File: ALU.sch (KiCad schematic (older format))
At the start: 54 parts, among them U501 74LS86AN, U502 74HCT32N, U503 74HCT32N, U504 74LS04, U505 74HCT157N, U506 74LS86AN, U507 74LS153, U508 74LS283N, U509 74HCT08N, U510 74HCT574N, U511 74LS283N, U512 74HCT541N, U513 74HCT08N, U514 74HCT574N, U515 74HCT541N, U516 74HCT08N, U517 74HCT74N, U518 74HCT74N

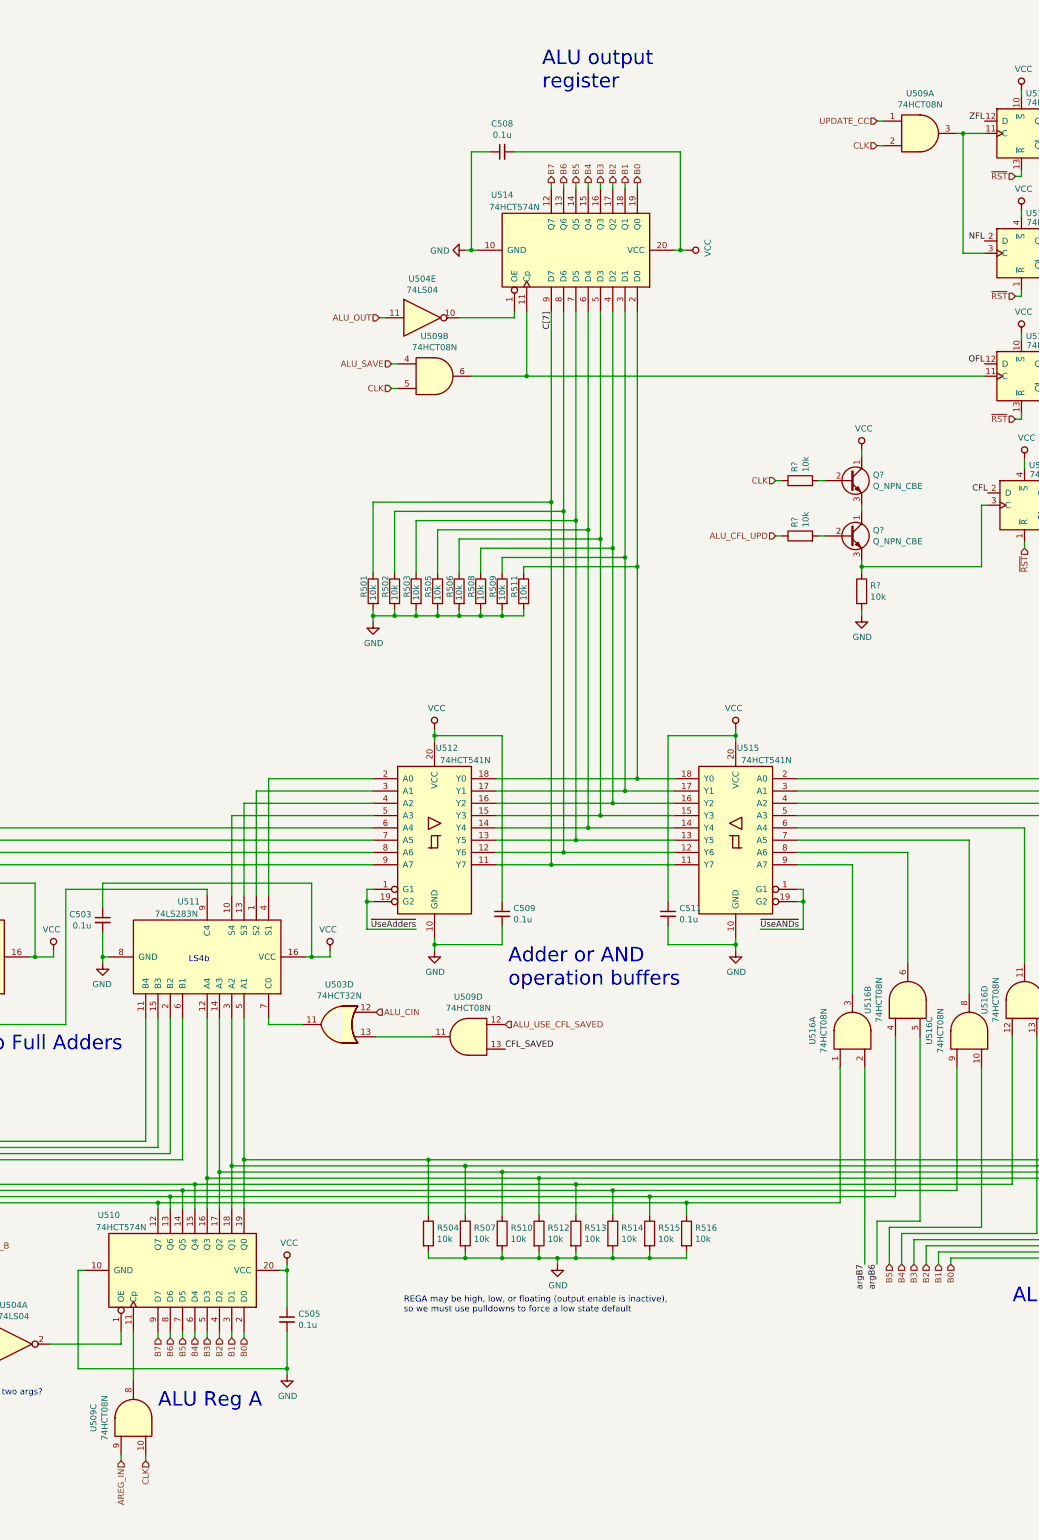
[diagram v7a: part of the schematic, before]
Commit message: Rearranged some generic logic gates in ALU to match physical net connections on the breadboard.
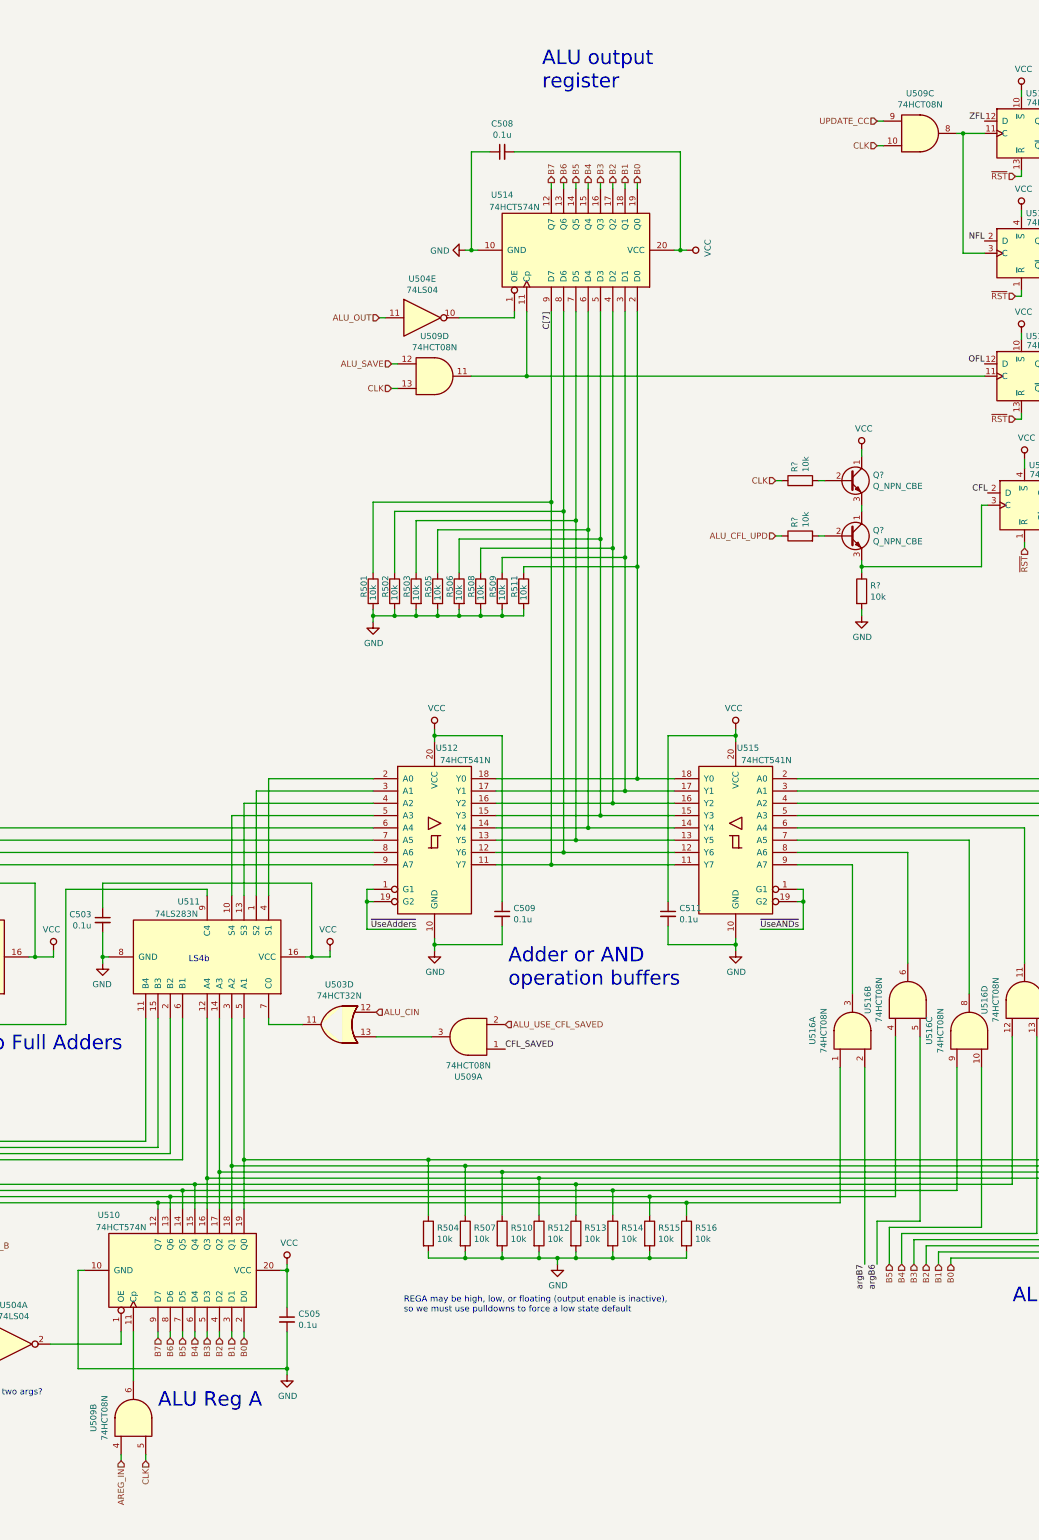
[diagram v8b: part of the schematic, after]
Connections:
- net ALU_SAVE: now also U509.12; no longer U509.4
- net ALU_USE_CFL_SAVED: now also U509.2; no longer U509.12
- net AREG_IN: now also U509.4; no longer U509.9
- net CFL_SAVED: now also U509.1; no longer U509.13
- net CLK: now also U509.13; no longer U509.2
- net UPDATE_CC: now also U509.9; no longer U509.1
- net at U514.11 (Cp), U517.11 (C): now also U509.11; no longer U509.6
- net at U518.11 (C), U518.3 (C): now also U509.8; no longer U509.3
- net at U503.13: now also U509.3; no longer U509.11
- net at U510.11 (Cp): now also U509.6; no longer U509.8
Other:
- moved on the sheet: U509A, U509B, U509C, U509D
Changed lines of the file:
@@
 L Breadboard_CPU-rescue:74LS08-74xx U509
 U 4 1 610C6B10
-P 10325 9600
-F 0 "U509" H 10325 9925 50  0000 C CNN
-F 1 "74HCT08N" H 10325 9834 50  0000 C CNN
-F 2 "" H 10325 9600 50  0001 C CNN
-F 3 "http://www.ti.com/lit/gpn/sn74LS08" H 10325 9600 50  0001 C CNN
-	4    10325 9600
-	-1   0    0    -1
+P 10050 4225
+F 0 "U509" H 10050 4550 50  0000 C CNN
+F 1 "74HCT08N" H 10050 4459 50  0000 C CNN
+F 2 "" H 10050 4225 50  0001 C CNN
+F 3 "http://www.ti.com/lit/gpn/sn74LS08" H 10050 4225 50  0001 C CNN
+	4    10050 4225
+	1    0    0    -1
 $EndComp
 Wire Wire Line
@@
 L Breadboard_CPU-rescue:74LS08-74xx U509
 U 3 1 610C6B0A
-P 7600 12700
-F 0 "U509" H 7600 13025 50  0000 C CNN
-F 1 "74HCT08N" H 7600 12934 50  0000 C CNN
-F 2 "" H 7600 12700 50  0001 C CNN
-F 3 "http://www.ti.com/lit/gpn/sn74LS08" H 7600 12700 50  0001 C CNN
-	3    7600 12700
-	0    -1   -1   0
+P 14000 2250
+F 0 "U509" H 14000 2575 50  0000 C CNN
+F 1 "74HCT08N" H 14000 2484 50  0000 C CNN
+F 2 "" H 14000 2250 50  0001 C CNN
+F 3 "http://www.ti.com/lit/gpn/sn74LS08" H 14000 2250 50  0001 C CNN
+	3    14000 2250
+	1    0    0    -1
 $EndComp
 $Comp
@@
 L Breadboard_CPU-rescue:74LS08-74xx U509
 U 2 1 61036CFD
-P 10050 4225
-F 0 "U509" H 10050 4550 50  0000 C CNN
-F 1 "74HCT08N" H 10050 4459 50  0000 C CNN
-F 2 "" H 10050 4225 50  0001 C CNN
-F 3 "http://www.ti.com/lit/gpn/sn74LS08" H 10050 4225 50  0001 C CNN
-	2    10050 4225
-	1    0    0    -1
+P 7600 12700
+F 0 "U509" H 7600 13025 50  0000 C CNN
+F 1 "74HCT08N" H 7600 12934 50  0000 C CNN
+F 2 "" H 7600 12700 50  0001 C CNN
+F 3 "http://www.ti.com/lit/gpn/sn74LS08" H 7600 12700 50  0001 C CNN
+	2    7600 12700
+	0    -1   -1   0
 $EndComp
 $Comp
@@
 L Breadboard_CPU-rescue:74LS08-74xx U509
 U 1 1 613F070E
-P 14000 2250
-F 0 "U509" H 14000 2575 50  0000 C CNN
-F 1 "74HCT08N" H 14000 2484 50  0000 C CNN
-F 2 "" H 14000 2250 50  0001 C CNN
-F 3 "http://www.ti.com/lit/gpn/sn74LS08" H 14000 2250 50  0001 C CNN
-	1    14000 2250
-	1    0    0    -1
+P 10325 9600
+F 0 "U509" H 10325 9925 50  0000 C CNN
+F 1 "74HCT08N" H 10325 9834 50  0000 C CNN
+F 2 "" H 10325 9600 50  0001 C CNN
+F 3 "http://www.ti.com/lit/gpn/sn74LS08" H 10325 9600 50  0001 C CNN
+	1    10325 9600
+	-1   0    0    1
 $EndComp
 Text HLabel 13650 2350 0    50   Input ~ 0
